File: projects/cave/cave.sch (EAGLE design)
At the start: 115 parts, among them U1 IRLML6344TRPBF, U10 IRLML6344TRPBF, U11 IRLML6344TRPBF, U12 IRLML6344TRPBF, U2 TLC555CDR, U3 IRLML6344TRPBF, U4 IRLML6344TRPBF, U5 IRLML6344TRPBF, U6 IRLML6344TRPBF, U7 TPS54625, U9 IRLML6344TRPBF

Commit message: finished routing 5V step down regulator
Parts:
- X2: device con-subd:F09H -> con-subd:F09V
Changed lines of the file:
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@@
 <part name="SMW5-2" library="SMW" deviceset="SMW530RJT" device="" value="30"/>
 <part name="SPM6530-1" library="SPM_inductor" deviceset="SPM6530" device="" value="1.5uH"/>
-<part name="X2" library="con-subd" deviceset="F09" device="H"/>
+<part name="X2" library="con-subd" deviceset="F09" device="V"/>
 <part name="X3" library="con-subd" deviceset="F25" device="V"/>
 </parts>

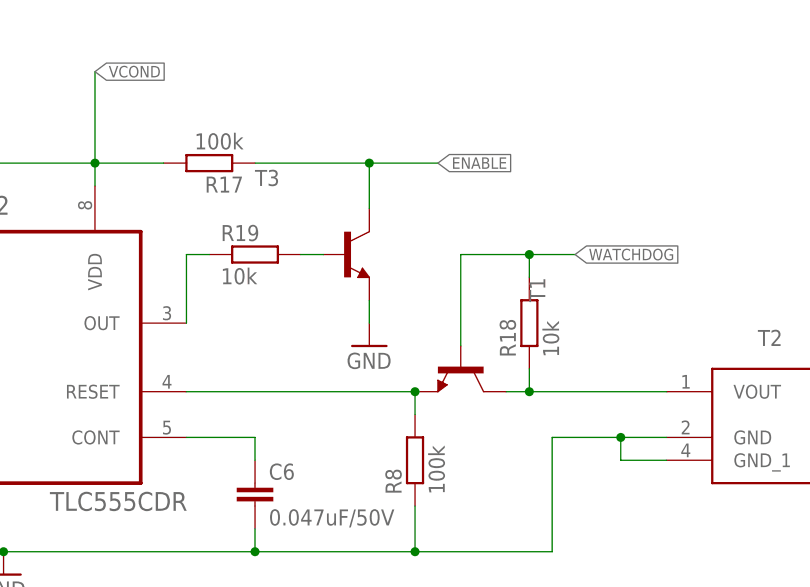
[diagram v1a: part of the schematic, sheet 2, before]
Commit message: 555 components placed but not routed. Updated 555 pin description in package.
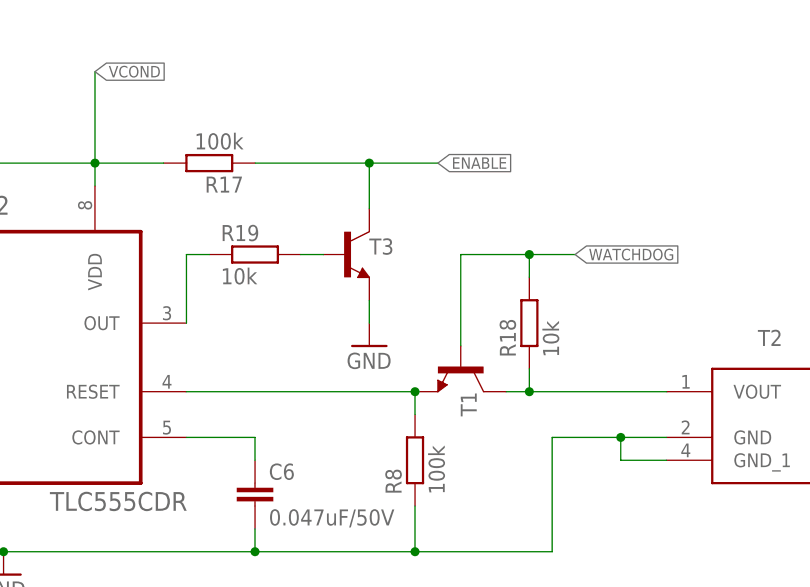
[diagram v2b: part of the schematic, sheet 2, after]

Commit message: WIP on "sensor" sector
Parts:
- removed SCREEN_5V, SCREEN_GND, UART_RX_5V, UART_TX_5V: WIREPAD3,81/1,4, wirepad:WIREPAD3,81/1,4
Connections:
- removed net N$18: R22.1, T4.E, UART_TX_5V.P
- removed net N$19: R20.2, UART_RX_5V.P
- net +5V: no longer SCREEN_5V.P
- net GND: no longer SCREEN_GND.P
- net UART_RX_5V: now also R20.2
- net UART_TX_5V: now also R22.1, T4.E
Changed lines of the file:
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@@
 <part name="R20" library="rcl" deviceset="R-EU_" device="R0603" value="100k"/>
 <part name="R21" library="rcl" deviceset="R-EU_" device="R0603" value="51k"/>
-<part name="UART_RX_5V" library="wirepad" deviceset="WIREPAD" device="3,81/1,4"/>
 <part name="GND10" library="supply1" deviceset="GND" device=""/>
 <part name="T4" library="transistor" deviceset="*-NPN-" device="SOT23-BEC" technology="MMBT2369LT1"/>
 <part name="R22" library="rcl" deviceset="R-EU_" device="R0603" value="10k"/>
-<part name="UART_TX_5V" library="wirepad" deviceset="WIREPAD" device="3,81/1,4"/>
-<part name="SCREEN_GND" library="wirepad" deviceset="WIREPAD" device="3,81/1,4"/>
-<part name="SCREEN_5V" library="wirepad" deviceset="WIREPAD" device="3,81/1,4"/>
 <part name="GND11" library="supply1" deviceset="GND" device=""/>
 <part name="R23" library="rcl" deviceset="R-EU_" device="R0603" value="10k"/>
@@
 <instance part="R20" gate="G$1" x="58.42" y="33.02" rot="R90"/>
 <instance part="R21" gate="G$1" x="58.42" y="17.78" rot="R90"/>
-<instance part="UART_RX_5V" gate="G$1" x="111.76" y="38.1" rot="R180"/>
 <instance part="GND10" gate="1" x="58.42" y="7.62"/>
 <instance part="T4" gate="G$1" x="55.88" y="66.04"/>
 <instance part="R22" gate="G$1" x="58.42" y="53.34" rot="R270"/>
-<instance part="UART_TX_5V" gate="G$1" x="111.76" y="58.42" rot="R180"/>
-<instance part="SCREEN_GND" gate="G$1" x="111.76" y="12.7" rot="R180"/>
-<instance part="SCREEN_5V" gate="G$1" x="111.76" y="73.66" rot="R180"/>
 <instance part="GND11" gate="1" x="58.42" y="43.18"/>
 <instance part="R23" gate="G$1" x="45.72" y="66.04"/>
@@
 <wire x1="58.42" y1="12.7" x2="109.22" y2="12.7" width="0.1524" layer="91"/>
 <junction x="58.42" y="12.7"/>
-<pinref part="SCREEN_GND" gate="G$1" pin="P"/>
+<label x="109.22" y="12.7" size="1.27" layer="95" xref="yes"/>
 </segment>
 <segment>
@@
 </segment>
 </net>
-<net name="N$19" class="0">
+<net name="UART_RX_5V" class="0">
 <segment>
 <pinref part="R20" gate="G$1" pin="2"/>
 <wire x1="58.42" y1="38.1" x2="109.22" y2="38.1" width="0.1524" layer="91"/>
-<pinref part="UART_RX_5V" gate="G$1" pin="P"/>
-</segment>
-</net>
-<net name="N$18" class="0">
+<label x="109.22" y="38.1" size="1.27" layer="95" xref="yes"/>
+</segment>
+</net>
+<net name="UART_TX_5V" class="0">
 <segment>
 <pinref part="R22" gate="G$1" pin="1"/>
 <pinref part="T4" gate="G$1" pin="E"/>
 <wire x1="58.42" y1="58.42" x2="58.42" y2="60.96" width="0.1524" layer="91"/>
-<pinref part="UART_TX_5V" gate="G$1" pin="P"/>
 <wire x1="109.22" y1="58.42" x2="58.42" y2="58.42" width="0.1524" layer="91"/>
 <junction x="58.42" y="58.42"/>
+<label x="109.22" y="58.42" size="1.27" layer="95" xref="yes"/>
 </segment>
 </net>
@@
 <wire x1="58.42" y1="71.12" x2="58.42" y2="73.66" width="0.1524" layer="91"/>
 <wire x1="58.42" y1="73.66" x2="109.22" y2="73.66" width="0.1524" layer="91"/>
-<pinref part="SCREEN_5V" gate="G$1" pin="P"/>
 <pinref part="SUPPLY14" gate="+5V" pin="+5V"/>
 <junction x="58.42" y="73.66"/>
-</segment>
-</net>
+<label x="109.22" y="73.66" size="1.27" layer="95" xref="yes"/>
+</segment>
+</net>

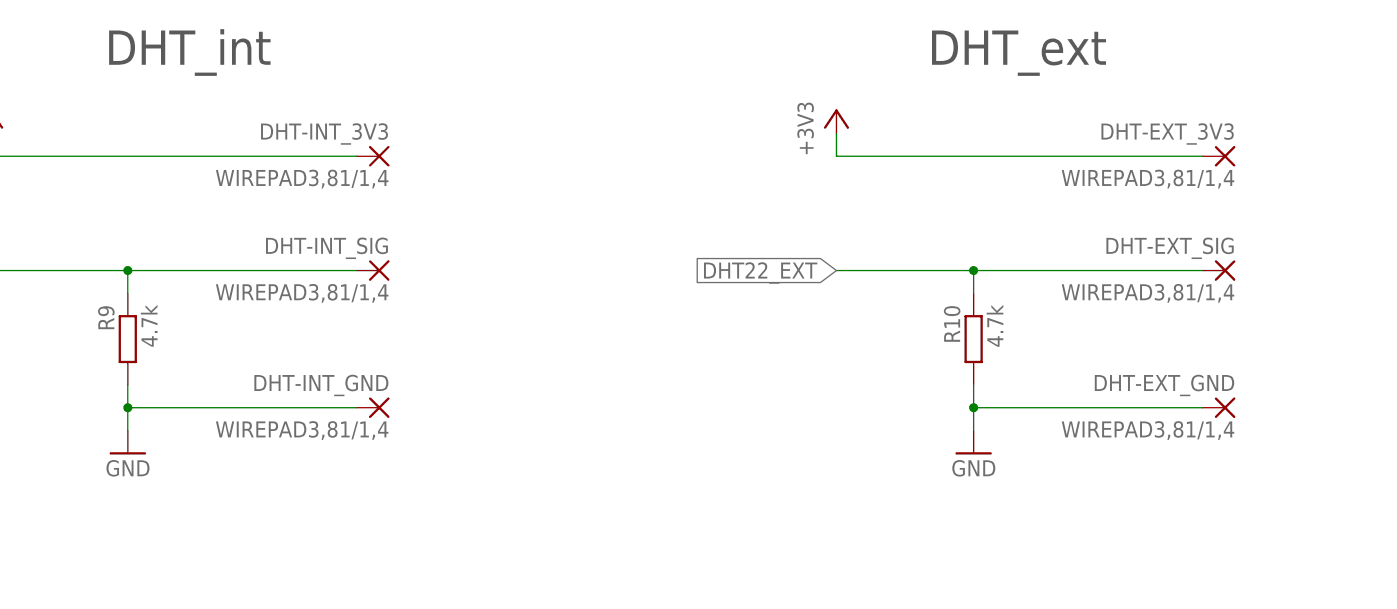
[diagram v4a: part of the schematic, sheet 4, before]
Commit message: Component layout in progress.
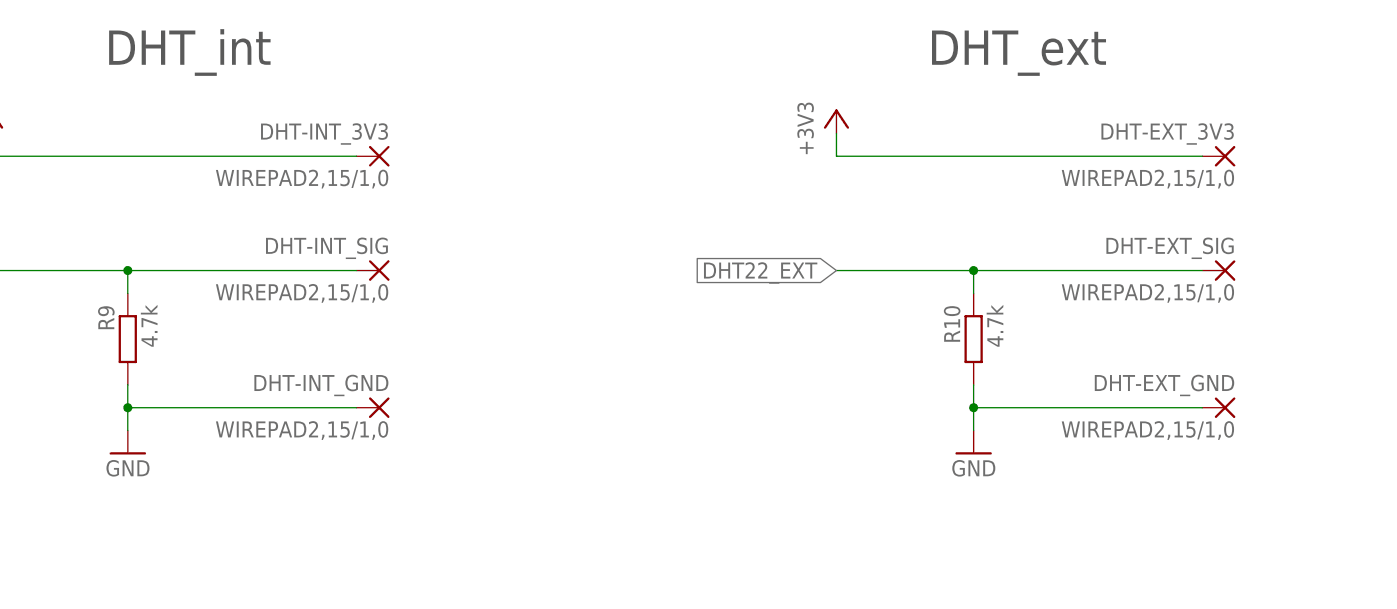
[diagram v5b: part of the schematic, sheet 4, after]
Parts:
- DHT-EXT_3V3, DHT-EXT_GND, DHT-EXT_SIG, DHT-INT_3V3, DHT-INT_GND, DHT-INT_SIG: value WIREPAD3,81/1,4 -> WIREPAD2,15/1,0; device wirepad:WIREPAD3,81/1,4 -> wirepad:WIREPAD2,15/1,0
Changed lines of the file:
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@@
 <grid distance="0.1" unitdist="inch" unit="inch" style="lines" multiple="1" display="no" altdistance="0.01" altunitdist="inch" altunit="inch"/>
 <layers>
-<layer number="1" name="Top" color="4" fill="1" visible="no" active="no"/>
-<layer number="2" name="Route2" color="1" fill="3" visible="no" active="no"/>
-<layer number="3" name="Route3" color="4" fill="3" visible="no" active="no"/>
-<layer number="14" name="Route14" color="1" fill="6" visible="no" active="no"/>
-<layer number="15" name="Route15" color="4" fill="6" visible="no" active="no"/>
-<layer number="16" name="Bottom" color="1" fill="1" visible="no" active="no"/>
-<layer number="17" name="Pads" color="2" fill="1" visible="no" active="no"/>
-<layer number="18" name="Vias" color="2" fill="1" visible="no" active="no"/>
-<layer number="19" name="Unrouted" color="6" fill="1" visible="no" active="no"/>
-<layer number="20" name="Dimension" color="15" fill="1" visible="no" active="no"/>
-<layer number="21" name="tPlace" color="7" fill="1" visible="no" active="no"/>
-<layer number="22" name="bPlace" color="7" fill="1" visible="no" active="no"/>
-<layer number="23" name="tOrigins" color="15" fill="1" visible="no" active="no"/>
-<layer number="24" name="bOrigins" color="15" fill="1" visible="no" active="no"/>
-<layer number="25" name="tNames" color="7" fill="1" visible="no" active="no"/>
-<layer number="26" name="bNames" color="7" fill="1" visible="no" active="no"/>
-<layer number="27" name="tValues" color="7" fill="1" visible="no" active="no"/>
-<layer number="28" name="bValues" color="7" fill="1" visible="no" active="no"/>
+<layer number="1" name="Top" color="4" fill="1" visible="yes" active="no"/>
+<layer number="2" name="Route2" color="1" fill="3" visible="yes" active="no"/>
+<layer number="3" name="Route3" color="4" fill="3" visible="yes" active="no"/>
+<layer number="14" name="Route14" color="1" fill="6" visible="yes" active="no"/>
+<layer number="15" name="Route15" color="4" fill="6" visible="yes" active="no"/>
+<layer number="16" name="Bottom" color="1" fill="1" visible="yes" active="no"/>
+<layer number="17" name="Pads" color="2" fill="1" visible="yes" active="no"/>
+<layer number="18" name="Vias" color="2" fill="1" visible="yes" active="no"/>
+<layer number="19" name="Unrouted" color="6" fill="1" visible="yes" active="no"/>
+<layer number="20" name="Dimension" color="15" fill="1" visible="yes" active="no"/>
+<layer number="21" name="tPlace" color="7" fill="1" visible="yes" active="no"/>
+<layer number="22" name="bPlace" color="7" fill="1" visible="yes" active="no"/>
+<layer number="23" name="tOrigins" color="15" fill="1" visible="yes" active="no"/>
+<layer number="24" name="bOrigins" color="15" fill="1" visible="yes" active="no"/>
+<layer number="25" name="tNames" color="7" fill="1" visible="yes" active="no"/>
+<layer number="26" name="bNames" color="7" fill="1" visible="yes" active="no"/>
+<layer number="27" name="tValues" color="7" fill="1" visible="yes" active="no"/>
+<layer number="28" name="bValues" color="7" fill="1" visible="yes" active="no"/>
 <layer number="29" name="tStop" color="7" fill="3" visible="no" active="no"/>
 <layer number="30" name="bStop" color="7" fill="6" visible="no" active="no"/>
@@
 <layer number="35" name="tGlue" color="7" fill="4" visible="no" active="no"/>
 <layer number="36" name="bGlue" color="7" fill="5" visible="no" active="no"/>
-<layer number="37" name="tTest" color="7" fill="1" visible="no" active="no"/>
-<layer number="38" name="bTest" color="7" fill="1" visible="no" active="no"/>
+<layer number="37" name="tTest" color="7" fill="1" visible="yes" active="no"/>
+<layer number="38" name="bTest" color="7" fill="1" visible="yes" active="no"/>
 <layer number="39" name="tKeepout" color="4" fill="11" visible="no" active="no"/>
 <layer number="40" name="bKeepout" color="1" fill="11" visible="no" active="no"/>
@@
 <layer number="44" name="Drills" color="7" fill="1" visible="no" active="no"/>
 <layer number="45" name="Holes" color="7" fill="1" visible="no" active="no"/>
-<layer number="46" name="Milling" color="3" fill="1" visible="no" active="no"/>
-<layer number="47" name="Measures" color="7" fill="1" visible="no" active="no"/>
-<layer number="48" name="Document" color="7" fill="1" visible="no" active="no"/>
-<layer number="49" name="Reference" color="7" fill="1" visible="no" active="no"/>
-<layer number="50" name="dxf" color="7" fill="1" visible="no" active="no"/>
-<layer number="51" name="tDocu" color="7" fill="1" visible="no" active="no"/>
-<layer number="52" name="bDocu" color="7" fill="1" visible="no" active="no"/>
-<layer number="53" name="tGND_GNDA" color="7" fill="9" visible="no" active="no"/>
-<layer number="54" name="bGND_GNDA" color="1" fill="9" visible="no" active="no"/>
-<layer number="56" name="wert" color="7" fill="1" visible="no" active="no"/>
-<layer number="59" name="Invisible" color="7" fill="1" visible="no" active="no"/>
-<layer number="61" name="stand" color="7" fill="1" visible="no" active="no"/>
+<layer number="46" name="Milling" color="3" fill="1" visible="yes" active="no"/>
+<layer number="47" name="Measures" color="7" fill="1" visible="yes" active="no"/>
+<layer number="48" name="Document" color="7" fill="1" visible="yes" active="no"/>
+<layer number="49" name="Reference" color="7" fill="1" visible="yes" active="no"/>
+<layer number="50" name="dxf" color="7" fill="1" visible="yes" active="no"/>
+<layer number="51" name="tDocu" color="7" fill="1" visible="yes" active="no"/>
+<layer number="52" name="bDocu" color="7" fill="1" visible="yes" active="no"/>
+<layer number="53" name="tGND_GNDA" color="7" fill="9" visible="yes" active="no"/>
+<layer number="54" name="bGND_GNDA" color="1" fill="9" visible="yes" active="no"/>
+<layer number="56" name="wert" color="7" fill="1" visible="yes" active="no"/>
+<layer number="59" name="Invisible" color="7" fill="1" visible="yes" active="no"/>
+<layer number="61" name="stand" color="7" fill="1" visible="yes" active="no"/>
 <layer number="90" name="Modules" color="5" fill="1" visible="yes" active="yes"/>
 <layer number="91" name="Nets" color="2" fill="1" visible="yes" active="yes"/>
@@
 <part name="R8" library="rcl" deviceset="R-EU_" device="R0603" value="100k"/>
 <part name="D4" library="semicon-smd-ipc" deviceset="D-" device="A1-C3" value="SBR160S23-7"/>
-<part name="DHT-INT_GND" library="wirepad" deviceset="WIREPAD" device="3,81/1,4"/>
-<part name="DHT-INT_SIG" library="wirepad" deviceset="WIREPAD" device="3,81/1,4"/>
-<part name="DHT-INT_3V3" library="wirepad" deviceset="WIREPAD" device="3,81/1,4"/>
+<part name="DHT-INT_GND" library="wirepad" deviceset="WIREPAD" device="2,15/1,0" value="WIREPAD2,15/1,0"/>
+<part name="DHT-INT_SIG" library="wirepad" deviceset="WIREPAD" device="2,15/1,0" value="WIREPAD2,15/1,0"/>
+<part name="DHT-INT_3V3" library="wirepad" deviceset="WIREPAD" device="2,15/1,0" value="WIREPAD2,15/1,0"/>
 <part name="R9" library="rcl" deviceset="R-EU_" device="R0603" value="4.7k"/>
-<part name="DHT-EXT_GND" library="wirepad" deviceset="WIREPAD" device="3,81/1,4"/>
-<part name="DHT-EXT_SIG" library="wirepad" deviceset="WIREPAD" device="3,81/1,4"/>
-<part name="DHT-EXT_3V3" library="wirepad" deviceset="WIREPAD" device="3,81/1,4"/>
+<part name="DHT-EXT_GND" library="wirepad" deviceset="WIREPAD" device="2,15/1,0" value="WIREPAD2,15/1,0"/>
+<part name="DHT-EXT_SIG" library="wirepad" deviceset="WIREPAD" device="2,15/1,0" value="WIREPAD2,15/1,0"/>
+<part name="DHT-EXT_3V3" library="wirepad" deviceset="WIREPAD" device="2,15/1,0" value="WIREPAD2,15/1,0"/>
 <part name="R10" library="rcl" deviceset="R-EU_" device="R0603" value="4.7k"/>
 <part name="OPTSEN-EMIT_GND" library="wirepad" deviceset="WIREPAD" device="3,81/1,4"/>
